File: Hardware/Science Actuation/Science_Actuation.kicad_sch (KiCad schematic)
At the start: 33 parts, among them J2 RJ45_LED_Shielded, Q10 AO3401A, Q9 BSS138, U2 Teensy4.1_DEV-16771

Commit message: Added quad encoders, servos, signal
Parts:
- added Conn6: Molex_SL_02, MRDT_Connectors:MOLEX_SL_02_Vertical, symbol MRDT_Connectors:Molex_SL_02
- added D10, D11, D12, D13, D8, D9: YELLOW, symbol Device:LED
- added D16: LED(B), LED_SMD:LED_0603_1608Metric_Pad1.05x0.95mm_HandSolder, symbol Device:LED
- added Q10: AO3401A, Package_TO_SOT_SMD:SOT-23, symbol Transistor_FET:AO3401A
- added Q9: BSS138, Package_TO_SOT_SMD:SOT-23, symbol Transistor_FET:BSS138
- added QuadEncode1, QuadEncode2, QuadEncode3: Molex_SL_04, symbol MRDT_Connectors:Molex_SL_04
- added R11, R12, R13, R14, R15, R16: 120, symbol Device:R
- added R36: 4.7k, Resistor_SMD:R_0603_1608Metric_Pad0.98x0.95mm_HandSolder, symbol Device:R
- added R37, R38: 10k, Resistor_SMD:R_0603_1608Metric_Pad0.98x0.95mm_HandSolder, symbol Device:R
- added R39: 1k, Resistor_SMD:R_0603_1608Metric_Pad0.98x0.95mm_HandSolder, symbol Device:R
- added Servo1, Servo2, Servo3: Molex_SL_03, symbol MRDT_Connectors:Molex_SL_03
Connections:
- net Peristaltic Pump is gone; now on net Pump1: Q9.1 (G), R36.1
- net +12V: now also Q10.2 (S), R37.1; no longer Conn2.1, Conn3.1, Conn4.1
- net +3V3: now also Conn2.1, Conn3.1, Conn4.1
- net GND: now also Conn6.2, D10.1 (K), D11.1 (K), D12.1 (K), D13.1 (K), D16.1 (K), D8.1 (K), D9.1 (K), Q9.2 (S), QuadEncode1.4, QuadEncode2.4, QuadEncode3.4, R36.2, Servo1.3, Servo2.3, Servo3.3; no longer Conn2.2, Conn3.2, Conn4.2
- net MOCO1: no longer Conn2.3
- net MOCO2: no longer Conn3.3
- net MOCO3: no longer Conn4.3
- net Pump1: now reaches U2.11 (MOSI)
- net Pump2: now reaches U2.12 (MISO)
- net Pump2: now also Q9.1 (G), R36.1
- net Servo_3: now reaches U2.13 (SCK)
- net Servo_3: now also Servo3.2
- net Servo_2: now reaches U2.14 (A0)
- net Servo_2: now also Servo2.2
- net Servo_1: now reaches U2.15 (A1)
- net Servo_1: now also Servo1.2
- net Encoder_1a: now reaches U2.23 (A9)
- net Encoder_1a: now also QuadEncode1.2, R11.2
- net Encoder_1b: now reaches U2.24 (A10)
- net Encoder_1b: now also QuadEncode1.3, R12.1
- net Encoder_2a: now reaches U2.25 (A11)
- net Encoder_2a: now also QuadEncode2.2, R13.2
- net Encoder_2b: now reaches U2.26 (A12)
- net Encoder_2b: now also QuadEncode2.3, R14.1
- net Encoder_3a: now reaches U2.27 (A13)
- net Encoder_3a: now also QuadEncode3.2, R15.2
- net Encoder_3b: now reaches U2.38 (A14)
- net Encoder_3b: now also QuadEncode3.3, R16.1
- new net: D10.2 (A), R13.1
- new net: D13.2 (A), R16.2
- new net: D12.2 (A), R15.1
- new net: Q10.1 (G), R37.2, R38.1
- new net: Conn6.1, Q10.3 (D), R39.2
- new net: D11.2 (A), R14.2
- new net: D16.2 (A), R39.1
- new net: D8.2 (A), R11.1
- new net: Q9.3 (D), R38.2
- new net: D9.2 (A), R12.2
- new net +5V: QuadEncode1.1, QuadEncode2.1, QuadEncode3.1, Servo1.1, Servo2.1, Servo3.1
- new net MOCO1_FWD: Conn2.2
- new net MOCO1_RVS: Conn2.3
- new net MOCO2_FWD: Conn3.2
- new net MOCO2_RVS: Conn3.3
- new net MOCO3_FWD: Conn4.2
- new net MOCO3_RVS: Conn4.3
- no-connect marks 49 -> 38
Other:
- note added: "Quadrature Encoder"
- note added: "Servos"

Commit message: Finished rev 1 schematic and assigned footprints
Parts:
- added C2, C3: 10uF, Capacitor_SMD:C_0603_1608Metric_Pad1.08x0.95mm_HandSolder, symbol Device:C
- added C4: 220uF, Capacitor_THT:CP_Radial_D6.3mm_P2.50mm, symbol Device:C
- added Conn13: Molex_SL_02, MRDT_Connectors:MOLEX_SL_02_Vertical, symbol MRDT_Connectors:Molex_SL_02
- added D15: ORANGE, LED_SMD:LED_0603_1608Metric_Pad1.05x0.95mm_HandSolder, symbol Device:LED
- added D16, D17, D18: Green, LED_SMD:LED_0603_1608Metric_Pad1.05x0.95mm_HandSolder, symbol Device:LED
- added D19, D20, D21, D22, D23, D24, D25, D26, D27, D28: Blue, LED_SMD:LED_0603_1608Metric_Pad1.05x0.95mm_HandSolder, symbol Device:LED
- added J2: Conn_01x02_Pin, symbol Connector:Conn_01x02_Pin
- added Q5: BSS138, Package_TO_SOT_SMD:SOT-23, symbol Transistor_FET:BSS138
- added R21, R24: 300, Resistor_SMD:R_0603_1608Metric_Pad0.98x0.95mm_HandSolder, symbol Device:R
- added R22: 1k, Resistor_SMD:R_0603_1608Metric_Pad0.98x0.95mm_HandSolder, symbol Device:R
- added R23, R25, R26, R27, R28, R29, R30, R31, R32, R33, R34: 120, Resistor_SMD:R_0603_1608Metric_Pad0.98x0.95mm_HandSolder, symbol Device:R
- added SW1, SW2, SW3, SW4, SW5, SW6, SW7, SW8, SW9: SW_Push, Button_Switch_SMD:SW_SPST_TL3305A, symbol Switch:SW_Push
- added SW10: SW_SPDT, Button_Switch_THT:SW_Slide_1P2T_CK_OS102011MS2Q, symbol Switch:SW_SPDT
- added U2: OKI, MRDT_Devices:OKI_Horizontal, symbol MRDT_Devices:OKI
- Conn1: footprint (none) -> MRDT_Connectors:Square_Anderson_2_H_Side_By_Side
- Conn10, Conn11, Conn6, Conn7, Conn8, Conn9: footprint (none) -> MRDT_Connectors:MOLEX_SL_02_Vertical
- Conn2, Conn3, Conn4, Servo1, Servo2, Servo3: footprint (none) -> MRDT_Connectors:MOLEX_SL_03_Vertical
- D10, D11, D12, D13, D2, D3, D4, D5, D6, D7, D8, D9: footprint (none) -> LED_SMD:LED_0603_1608Metric_Pad1.05x0.95mm_HandSolder
- D16: value LED(B) -> Orange
- QuadEncode1, QuadEncode2, QuadEncode3: footprint (none) -> MRDT_Connectors:MOLEX_SL_04_Vertical
- R10, R11, R12, R13, R14, R15, R16, R5, R6, R7, R8, R9: footprint (none) -> Resistor_SMD:R_0603_1608Metric_Pad0.98x0.95mm_HandSolder
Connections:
- net MOCO1 is gone; now on net MOCO1_FWD: U2.0 (RX1)
- net MOCO2 is gone; now on net MOCO2_FWD: U2.1 (TX1)
- net MOCO3 is gone; now on net MOCO3_FWD: U2.7 (RX2)
- net +12V: now also C2.1, C4.1, R22.1, U2.1 (Vi)
- net +3V3: now also D28.2 (A), R23.1, SW1.1, SW10.1 (A), SW2.1, SW3.1, SW4.1, SW5.1, SW6.1, SW7.1, SW8.1, SW9.1
- net +5V: now also C3.1, Conn13.1, D15.2 (A), R24.1, U2.3 (Vo)
- net GND: now also C2.2, C3.2, C4.2, D16.1 (K), D17.1 (K), D18.1 (K), D19.1 (K), D20.1 (K), D21.1 (K), D22.1 (K), D23.1 (K), D24.1 (K), D25.1 (K), D26.1 (K), D27.1 (K), Q5.2 (S), SW10.3 (C), U2.2 (GND)
- net MOCO1_RVS: now also U2.8 (TX2)
- net MOCO2_RVS: now also U2.28 (RX7)
- net MOCO3_RVS: now also U2.29 (TX7)
- net SW7: now reaches U2.16 (A2)
- net SW7: now also R31.1, SW7.2
- net SW6: now reaches U2.17 (A3)
- net SW6: now also R30.1, SW6.2
- net SW5: now reaches U2.18 (A4)
- net SW5: now also R29.1, SW5.2
- net SW4: now reaches U2.19 (A5)
- net SW4: now also R28.1, SW4.2
- net SW3: now reaches U2.20 (A6)
- net SW3: now also R27.1, SW3.2
- net SW2: now reaches U2.21 (A7)
- net SW2: now also R26.1, SW2.2
- net SW1: now reaches U2.22 (A8)
- net SW1: now also R25.1, SW1.2
- net DIR_SW: now reaches U2.3 (LRCLK2)
- net DIR_SW: now also R34.2, SW10.2 (B)
- net SW8: now reaches U2.33 (MCLK2)
- net SW8: now also R32.1, SW8.2
- net LAS: now reaches U2.39 (A15)
- net LAS: now also Q5.1 (G)
- net SW9: now reaches U2.4 (BCLK2)
- net SW9: now also R33.1, SW9.2
- net Heater_Temp: now reaches U2.40 (A16)
- net Heater_Temp: now also J2.2 (Pin_2)
- net Heater_On: now reaches U2.41 (A17)
- net Heater_On: now also J2.1 (Pin_1)
- new net: D25.2 (A), R31.2
- new net: D26.2 (A), R32.2
- new net: D27.2 (A), R33.2
- new net: D22.2 (A), R28.2
- new net: Conn13.2, Q5.3 (D), R21.2
- new net: D17.2 (A), R23.2
- new net: D20.2 (A), R26.2
- new net: D28.1 (K), R34.1
- new net: D19.2 (A), R25.2
- new net: D23.2 (A), R29.2
- new net: D15.1 (K), R21.1
- new net: D24.2 (A), R30.2
- new net: D16.2 (A), R22.2
- new net: D21.2 (A), R27.2
- new net: D18.2 (A), R24.2
- no-connect marks 38 -> 23
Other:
- note added: "BUCK CONVERTER"
- note added: "BUTTON"
- note added: "LASER"
- note added: "LEDs"

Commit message: Boxed all components; edited heater schematic from a 2 pin connector to three pin, including all the previous connections but also adding a 5v supply
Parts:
- removed J2: Conn_01x02_Pin, symbol Connector:Conn_01x02_Pin
- added J3: Conn_01x03_Pin, symbol Connector:Conn_01x03_Pin
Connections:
- net +5V: now also J3.1 (Pin_1)
- net Heater_On: now also J3.2 (Pin_2)
- net Heater_Temp: now also J3.3 (Pin_3)
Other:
- note added: "BUTTONS"
- note added: "Heater"
- note added: "NOTE: ASSIGN FOOTPRINT TO 3 PIN CONNECTOR"
- note added: "Pumps"
- note removed: "BUTTON"
- note removed: "Peristaltic Pump"
- moved on the sheet: C2, C3, C4, Conn10, Conn11, Conn13, Conn1A, Conn1B, Conn2, Conn3, Conn4, Conn6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

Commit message: Completed BOM
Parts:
- removed J3: Conn_01x03_Pin, symbol Connector:Conn_01x03_Pin
- added Conn14: Molex_SL_03, MRDT_Connectors:MOLEX_SL_03_Vertical, symbol MRDT_Connectors:Molex_SL_03
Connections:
- net +5V: now also Conn14.3
- net Heater_On: now also Conn14.2
- net Heater_Temp: now also Conn14.1
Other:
- note removed: "NOTE: ASSIGN FOOTPRINT TO 3 PIN CONNECTOR"
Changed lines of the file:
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@@
     (effects (font (size 3.81 3.81)) (justify left bottom))
   )
-  (text "NOTE: ASSIGN FOOTPRINT TO 3 PIN CONNECTOR" (at 127 275.59 0)
-    (effects (font (size 1.27 1.27)) (justify left bottom))
-  )
   (text "LIMIT SWITCH CONNECTORS" (at 93.98 265.43 0)
     (effects (font (size 3.81 3.81)) (justify right bottom))
@@
     )
   )
-  (symbol (lib_id "Connector:Conn_01x03_Pin") (at 139.7 257.81 0) (unit 1)
-    (in_bom yes) (on_board yes) (dnp no) (fields_autoplaced)
-    (property "Reference" "J3" (at 140.335 250.19 0)
-      (effects (font (size 1.27 1.27)))
-    )
-    (property "Value" "Conn_01x03_Pin" (at 140.335 252.73 0)
-      (effects (font (size 1.27 1.27)))
-    )
-    (property "Footprint" "" (at 139.7 257.81 0)
-      (effects (font (size 1.27 1.27)) hide)
-    )
-    (property "Datasheet" "~" (at 139.7 257.81 0)
-      (effects (font (size 1.27 1.27)) hide)
-    )
-    (pin "1")
-    (pin "2")
-    (pin "3")
-    (instances
-      (project "Science_Actuation"
-        (path "/a309c31d-a907-45c3-9170-b69a69763088"
-          (reference "J3") (unit 1)
-        )
-      )
-    )
-  )
   (symbol (lib_id "Device:R") (at 137.16 320.04 0) (unit 1)
     (in_bom yes) (on_board yes) (dnp no) (fields_autoplaced)
@@
         )
       )
+    )
+  )
+  (symbol (lib_id "MRDT_Connectors:Molex_SL_03") (at 139.7 254 180) (unit 1)
+    (in_bom yes) (on_board yes) (dnp no) (fields_autoplaced)
+    (property "Reference" "Conn14" (at 138.43 248.92 0)
+      (effects (font (size 1.524 1.524)))
+    )
+    (property "Value" "Molex_SL_03" (at 138.43 251.46 0)
+      (effects (font (size 1.524 1.524)))
+    )
+    (property "Footprint" "MRDT_Connectors:MOLEX_SL_03_Vertical" (at 139.7 254 0)
+      (effects (font (size 1.524 1.524)) hide)
+    )
+    (property "Datasheet" "" (at 139.7 254 0)
+      (effects (font (size 1.524 1.524)) hide)
+    )
+    (pin "1")
+    (pin "2")
+    (pin "3")
+    (instances
+      (project "Science_Actuation"
+        (path "/a309c31d-a907-45c3-9170-b69a69763088"
+          (reference "Conn14") (unit 1)
+        )
+      )

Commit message: Fixed Board for Review
Changed various aspects, such as adding Mounting Holes, replacing 120Ohm resistors for 100Ohm, added footnotes, changed Heater from Comic Sans to default, etc.
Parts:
- removed C2, C3: 10uF, Capacitor_SMD:C_0603_1608Metric_Pad1.08x0.95mm_HandSolder, symbol Device:C
- removed C3: 0.1uF, Capacitor_SMD:C_0603_1608Metric_Pad1.08x0.95mm_HandSolder, symbol Device:C
- removed unit 2 of Conn1
- removed Conn10, Conn11, Conn13, Conn6 (x3), Conn9: Molex_SL_02, MRDT_Connectors:MOLEX_SL_02_Vertical, symbol MRDT_Connectors:Molex_SL_02
- removed Conn14, Conn2, Conn3, Conn4: Molex_SL_03, MRDT_Connectors:MOLEX_SL_03_Vertical, symbol MRDT_Connectors:Molex_SL_03
- removed D10, D11: YELLOW, LED_SMD:LED_0603_1608Metric_Pad1.05x0.95mm_HandSolder, symbol Device:LED
- removed D16 (x2): Orange, LED_SMD:LED_0603_1608Metric_Pad1.05x0.95mm_HandSolder, symbol Device:LED
- removed D16: Green, LED_SMD:LED_0603_1608Metric_Pad1.05x0.95mm_HandSolder, symbol Device:LED
- removed Q10 (x2): AO3401A, Package_TO_SOT_SMD:SOT-23, symbol Transistor_FET:AO3401A
- removed Q5, Q9 (x2): BSS138, Package_TO_SOT_SMD:SOT-23, symbol Transistor_FET:BSS138
- removed R11, R12, R13, R14, R16, R8, R9: 120, Resistor_SMD:R_0603_1608Metric_Pad0.98x0.95mm_HandSolder, symbol Device:R
- removed R36 (x2): 4.7k, Resistor_SMD:R_0603_1608Metric_Pad0.98x0.95mm_HandSolder, symbol Device:R
- removed R37 (x2), R38 (x2): 10k, Resistor_SMD:R_0603_1608Metric_Pad0.98x0.95mm_HandSolder, symbol Device:R
- removed R39 (x2): 1k, Resistor_SMD:R_0603_1608Metric_Pad0.98x0.95mm_HandSolder, symbol Device:R
- added C1: 220uF, Capacitor_THT:CP_Radial_D6.3mm_P2.50mm, symbol Device:C
- added C3: 10uF, Capacitor_SMD:C_0603_1608Metric_Pad1.08x0.95mm_HandSolder, symbol Device:C
- added C3: 0.1uF, Capacitor_SMD:C_0603_1608Metric_Pad1.08x0.95mm_HandSolder, symbol Device:C
- added unit 3 of Conn1
- added Conn10, Conn11, Conn9: Molex_SL_03, MRDT_Connectors:MOLEX_SL_03_Vertical, symbol MRDT_Connectors:Molex_SL_03
- added Conn2, Conn3, Conn4, Conn5, Conn6 (x3): Molex_SL_02, MRDT_Connectors:MOLEX_SL_02_Vertical, symbol MRDT_Connectors:Molex_SL_02
- added D1: ORANGE, LED_SMD:LED_0603_1608Metric_Pad1.05x0.95mm_HandSolder, symbol Device:LED
- added D14, D16: Blue, LED_SMD:LED_0603_1608Metric_Pad1.05x0.95mm_HandSolder, symbol Device:LED
- added D16 (x2): Orange, LED_SMD:LED_0603_1608Metric_Pad1.05x0.95mm_HandSolder, symbol Device:LED
- added H1, H2, H3, H4: MountingHole, MRDT_Drill_Holes:4_40_Hole_Corner, symbol Mechanical:MountingHole
- added J1, J2, J3: Conn_01x03_Pin, MRDT_Connectors:MOLEX_SL_03_Horizontal, symbol Connector:Conn_01x03_Pin
- added Q1, Q9 (x2): BSS138, Package_TO_SOT_SMD:SOT-23, symbol Transistor_FET:BSS138
- added Q10 (x2): AO3401A, Package_TO_SOT_SMD:SOT-23, symbol Transistor_FET:AO3401A
- added R1: 300, Resistor_SMD:R_0603_1608Metric_Pad0.98x0.95mm_HandSolder, symbol Device:R
- added R18, R19, R2, R20, R3, R4: 100, Resistor_SMD:R_0603_1608Metric_Pad0.98x0.95mm_HandSolder, symbol Device:R
- added R36 (x2): 4.7k, Resistor_SMD:R_0603_1608Metric_Pad0.98x0.95mm_HandSolder, symbol Device:R
- added R37 (x2), R38 (x2): 10k, Resistor_SMD:R_0603_1608Metric_Pad0.98x0.95mm_HandSolder, symbol Device:R
- added R39 (x2): 1k, Resistor_SMD:R_0603_1608Metric_Pad0.98x0.95mm_HandSolder, symbol Device:R
- C4: value 220uF -> 10uF; footprint Capacitor_THT:CP_Radial_D6.3mm_P2.50mm -> Capacitor_SMD:C_0603_1608Metric_Pad1.08x0.95mm_HandSolder
- D12, D8, D9: value YELLOW -> Green
- D13: value YELLOW -> Blue
- D15: value ORANGE -> Blue
- D17, D18: value Green -> Blue
- D23, D24, D25, D26, D27, D28: value Blue -> YELLOW
- R10: value 120 -> 300
- R15: value 120 -> 1k
- R21, R24: value 300 -> 100
- R22: value 1k -> 100
- R23, R25, R26, R27, R28, R29, R30, R31, R32, R33, R34, R5, R6, R7: value 120 -> 100
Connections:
- net +12V: now also R15.1, C1.1, C3.1, Conn1.3 (V+Act), Q10.2 (S), Q10.2 (S), R37.1, R37.1; no longer C4.1, R22.1
- net +3V3: now also D13.2 (A), Conn10.1, Conn11.1, Conn3.1, Conn4.1, Conn5.1, Conn6.1, Conn9.1, R18.1; no longer D28.2 (A), R23.1
- net +5V: now also C4.1, R10.1, Conn2.1, D1.2 (A); no longer D15.2 (A), R24.1
- net DIR_SW: now also R28.2; no longer R34.2
- net Encoder_1a: now also R29.2
- net Encoder_1b: now also R30.1
- net Encoder_2a: now also R31.2
- net Encoder_2b: now also R32.1
- net Encoder_3a: now also R33.2; no longer R15.2
- net Encoder_3b: now also R34.1
- net GND: now also D15.1 (K), D28.1 (K), C1.2, C3.1, C3.2, Conn6.2, Conn6.2, D14.1 (K), D16.1 (K), D16.1 (K), D16.1 (K), Q1.2 (S), Q9.2 (S), Q9.2 (S), R36.2, R36.2; no longer D13.1 (K)
- net Heater_On: now also J1.2 (Pin_2)
- net Heater_Temp: now also J1.3 (Pin_3)
- net LAS: now also Q1.1 (G)
- net LimitSwitch1: now also Conn3.2, R2.2; no longer R5.2
- net LimitSwitch2: now also Conn4.2, R3.2; no longer Conn7.2, R6.2
- net LimitSwitch3: now also Conn5.2, R4.2; no longer Conn8.2, R7.2
- net LimitSwitch4: now also R5.2, Conn6.2
- net LimitSwitch5: now also Conn7.2, R6.2
- net LimitSwitch6: now also Conn8.2, R7.2; no longer R10.2
- net MOCO1_FWD: now also Conn9.2
- net MOCO1_RVS: now also Conn9.3
- net MOCO2_FWD: now also Conn10.2
- net MOCO2_RVS: now also Conn10.3
- net MOCO3_FWD: now also Conn11.2
- net MOCO3_RVS: now also Conn11.3
- net Pump1: now also Q9.1 (G), R36.1
- net Pump2: now also Q9.1 (G), R36.1
- net SW1: now also R19.1; no longer R25.1
- net SW2: now also R20.1; no longer R26.1
- net SW3: now also R21.1; no longer R27.1
- net SW4: now also R22.1; no longer R28.1
- net SW5: now also R23.1; no longer R29.1
- net SW6: now also R24.1; no longer R30.1
- net SW7: now also R25.1; no longer R31.1
- net SW8: now also R26.1; no longer R32.1
- net SW9: now also R27.1; no longer R33.1
- net at D5.2 (A): now also R5.1
- net at D25.2 (A): now also R31.1; no longer R31.2
- net at D3.2 (A): now also R3.1; no longer R6.1
- net at D12.2 (A): now also R18.2; no longer R15.1
- net at D27.2 (A): now also R33.1; no longer R33.2
- net at D22.2 (A): now also R27.2; no longer R28.2
- net at D7.2 (A): now also R7.1; no longer R10.1
- net at R21.2: now also D16.2 (A)
- net at R23.2: now also D18.2 (A); no longer D17.2 (A)
- net at D20.2 (A): now also R25.2; no longer R26.2
- net at D19.2 (A): now also R24.2; no longer R25.2
- net at J2.2, J2.5: now also C3.2
- net at D6.2 (A): now also R6.1
- net at D23.2 (A): now also R29.1; no longer R29.2
- net at D8.2 (A): now also R10.2
- net at D2.2 (A): now also R2.1; no longer R5.1
- net at R22.2: now also D17.2 (A)
- net Heater_Temp2: now reaches U2.2 (OUT2)
- net Heater_Temp2: now also J2.3 (Pin_3)
- net Heater_On3: now reaches U2.32 (OUT1B)
- net Heater_On3: now also J3.2 (Pin_2)
- net Heater_Temp3: now reaches U2.6 (OUT1D)
- net Heater_Temp3: now also J3.3 (Pin_3)
- net Heater_On2: now reaches U2.9 (OUT1C)
- net Heater_On2: now also J2.2 (Pin_2)
- net LED: now reaches J2.10, U2.LED
- net at D21.2 (A): now also R26.2; no longer R27.2
- net at D9.2 (A): now also R15.2
- net at D4.2 (A): now also R4.1; no longer R7.1
- new net: D14.2 (A), R19.2
- new net: Q9.3 (D), R38.2 (x2)
- new net: Q10.1 (G), R37.2, R38.1 (x2)
- new net: D1.1 (K), R1.1
- new net: D28.2 (A), R34.2
- new net: D16.2 (A), R39.1 (x2)
- new net: Conn6.1, Q10.3 (D), R39.2 (x2)
- new net: Conn2.2, Q1.3 (D), R1.2
- new net: D15.2 (A), R20.2
- new net: D13.1 (K), R28.1
- new net +3.3V: J1.1 (Pin_1), J2.1 (Pin_1), J3.1 (Pin_1)
- no-connect marks 23 -> 19

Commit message: Fixed Remaining things from the schematic review
Changing schematic size, added flags to Teensy, removed Science Motor Controller
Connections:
- net +5V: now also U2.VIN
- net LimitSwitch1: now also U2.34 (RX8)
- net LimitSwitch2: now also U2.35 (TX8)
- net LimitSwitch3: now also U2.30 (CRX3)
- net LimitSwitch4: now also U2.31 (CTX3)
- net LimitSwitch5: now also U2.37 (CS3)
- net LimitSwitch6: now also U2.36 (CS2)
- no-connect marks 19 -> 12
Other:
- note added: "RJ45 Ethernet"
- note added: "Teensy"
- moved on the sheet: C1, C3, C4, Conn10, Conn11, Conn1A, Conn1C, Conn2, Conn3, Conn4, Conn5, Conn6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

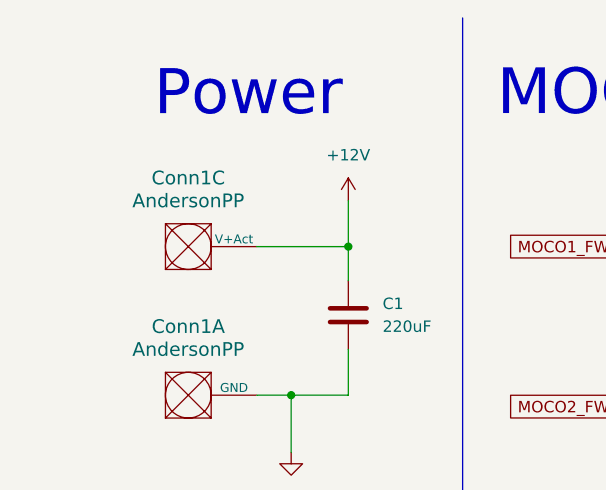
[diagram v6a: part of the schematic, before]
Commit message: Changed anderson to logic, edited BOM
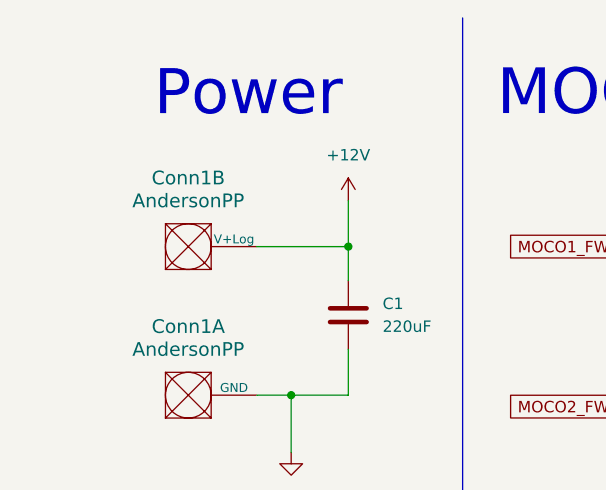
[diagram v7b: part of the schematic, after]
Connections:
- net +12V: now also Conn1.2 (V+Log); no longer Conn1.3 (V+Act)
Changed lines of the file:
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@@
     )
   )
-  (symbol (lib_id "MRDT_Connectors:AndersonPP") (at 20.32 39.37 0) (unit 3)
+  (symbol (lib_id "MRDT_Connectors:AndersonPP") (at 20.32 39.37 0) (unit 2)
     (in_bom yes) (on_board yes) (dnp no) (fields_autoplaced)
     (property "Reference" "Conn1" (at 22.86 29.21 0)
@@
       (project "Science_Actuation"
         (path "/a309c31d-a907-45c3-9170-b69a69763088"
-          (reference "Conn1") (unit 3)
+          (reference "Conn1") (unit 2)
         )
       )
